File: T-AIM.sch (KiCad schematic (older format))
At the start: 40 parts, among them IC1 ATMEGA328PB-A, J1 ADXL345 Connector, J2 PIR Sensor Connector, J3 JY-MCU HC-05 Pins, J4 CONN_01X03, J5 CONN_01X02, J6 CONN_01X03, SW1 Connection Button, SW2 Reset Button, U1 TPS61200

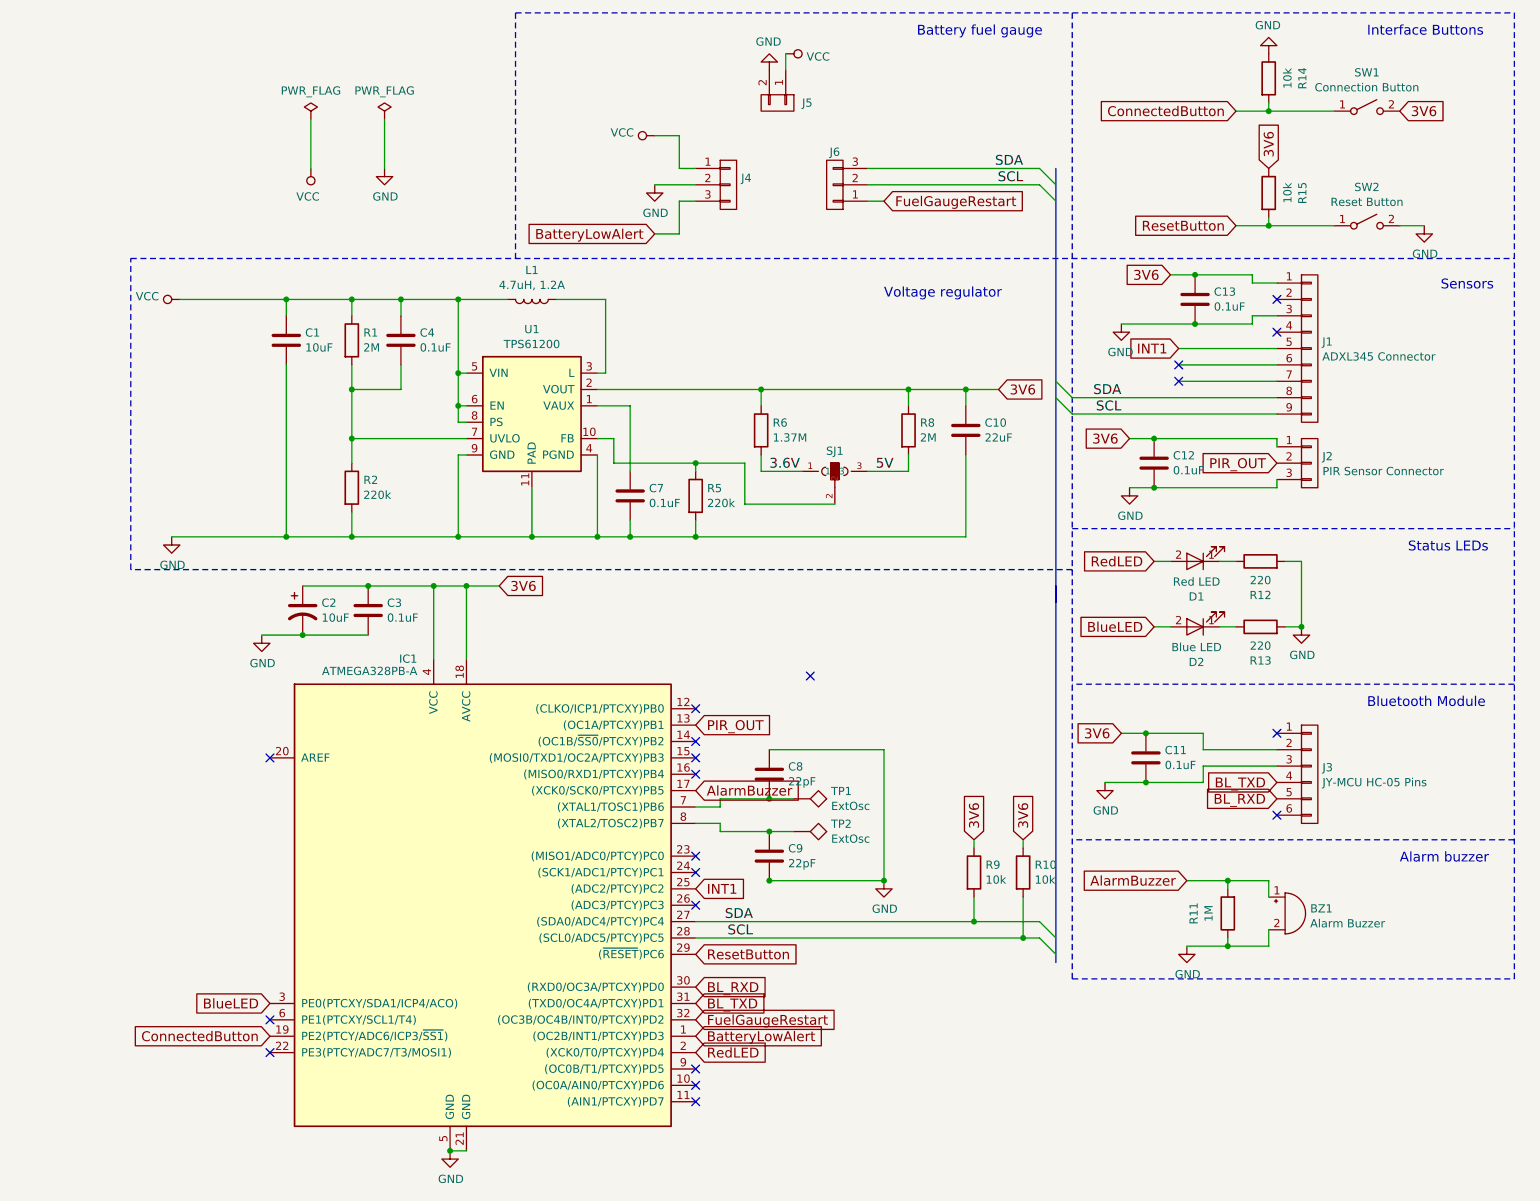
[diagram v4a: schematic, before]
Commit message: v0.3: 3.9V field shrunk; Added ISP header; Fixed fuel gauge pin shortcut :P
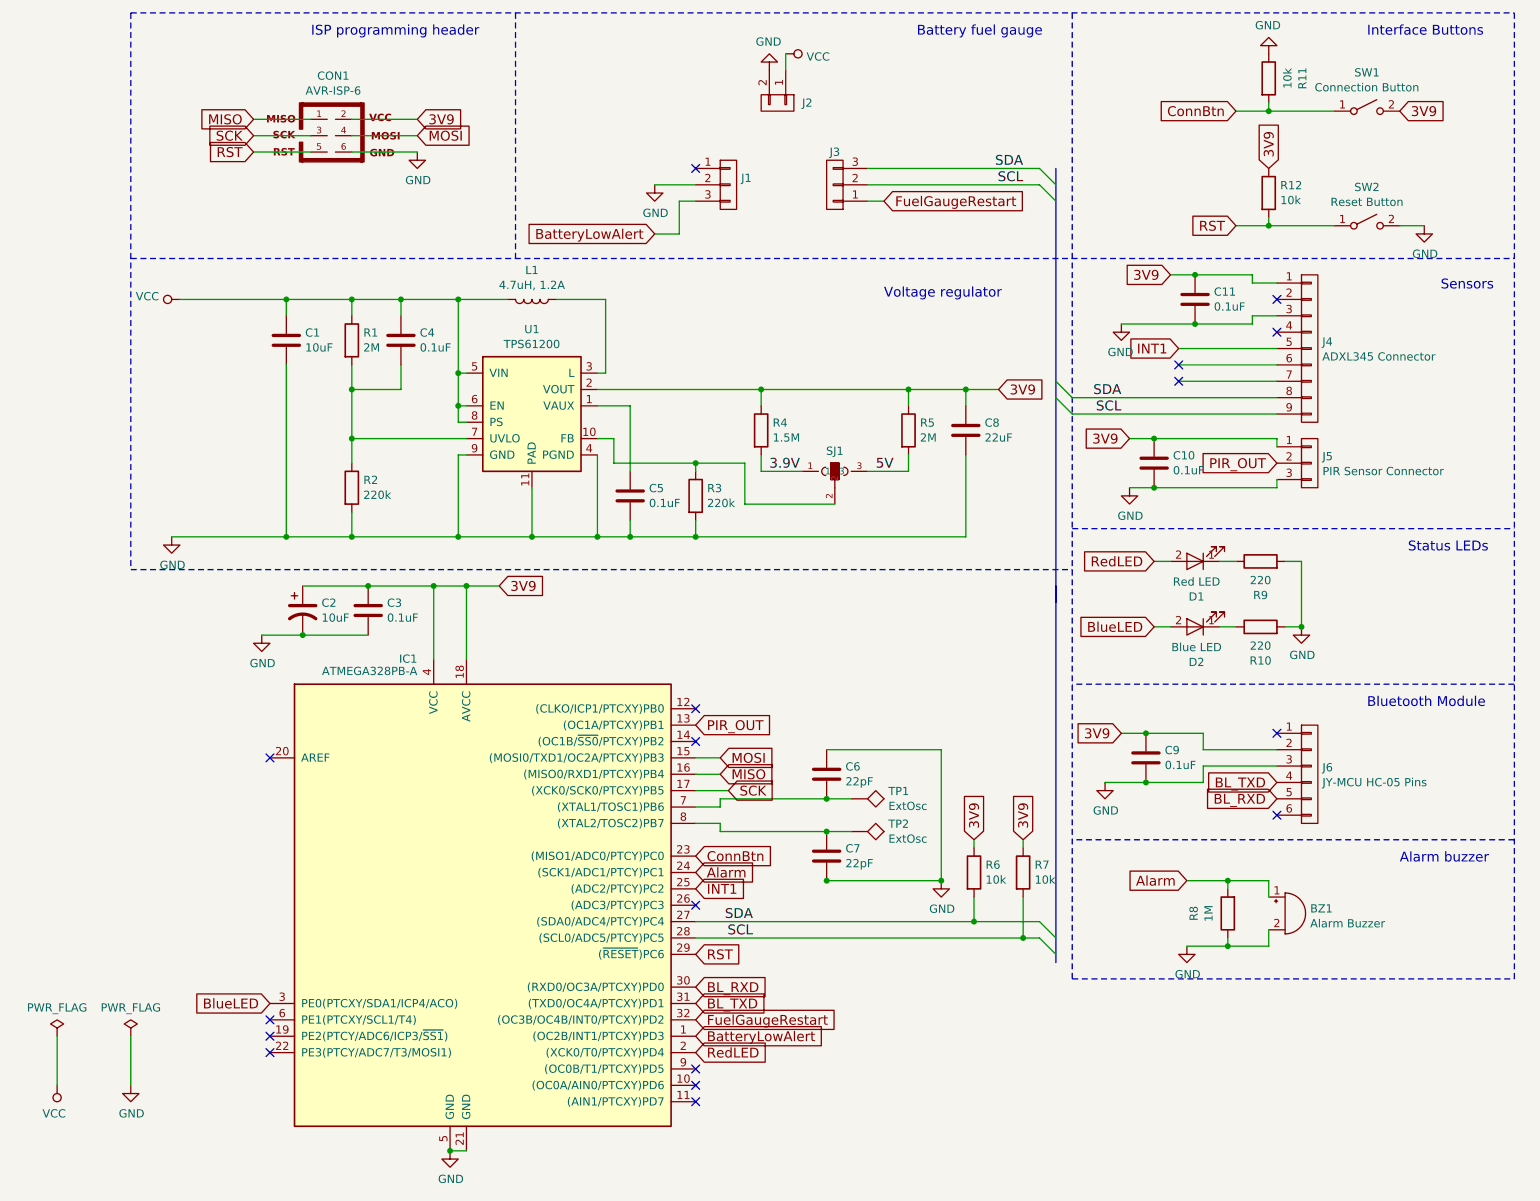
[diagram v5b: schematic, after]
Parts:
- added CON1: AVR-ISP-6, T-AIM:2X3-SHROUDED, symbol AVR-ISP-6
- C1, C3, C4: footprint Capacitors_SMD:C_1812_HandSoldering -> Capacitors_SMD:C_1206_HandSoldering
- C10: renamed from C12; footprint Capacitors_SMD:C_1812_HandSoldering -> Capacitors_SMD:C_1206_HandSoldering
- C11: renamed from C13; footprint Capacitors_SMD:C_1812_HandSoldering -> Capacitors_SMD:C_1206_HandSoldering
- C5: renamed from C7; footprint Capacitors_SMD:C_1812_HandSoldering -> Capacitors_SMD:C_1206_HandSoldering
- C6: renamed from C8; footprint Capacitors_SMD:C_1812_HandSoldering -> Capacitors_SMD:C_0603_HandSoldering
- C7: renamed from C9; footprint Capacitors_SMD:C_1812_HandSoldering -> Capacitors_SMD:C_0603_HandSoldering
- C8: renamed from C10; footprint Capacitors_SMD:C_1812_HandSoldering -> Capacitors_SMD:C_1206_HandSoldering
- C9: renamed from C11; footprint Capacitors_SMD:C_1812_HandSoldering -> Capacitors_SMD:C_1210_HandSoldering
- J6: renamed from J3; footprint Pin_Headers:Pin_Header_Straight_1x06_Pitch2.00mm -> Pin_Headers:Pin_Header_Straight_1x06_Pitch2.54mm
- R10: renamed from R13; footprint Resistors_SMD:R_0805_HandSoldering -> Resistors_SMD:R_1206_HandSoldering
- R11: renamed from R14; footprint Resistors_SMD:R_0805_HandSoldering -> Resistors_SMD:R_1206_HandSoldering
- R12: renamed from R15; footprint Resistors_SMD:R_0805_HandSoldering -> Resistors_SMD:R_1206_HandSoldering
- R4: renamed from R6; value 1.37M -> 1.5M
- R6: renamed from R9; footprint Resistors_SMD:R_0805_HandSoldering -> Resistors_SMD:R_1206_HandSoldering
- R7: renamed from R10; footprint Resistors_SMD:R_0805_HandSoldering -> Resistors_SMD:R_1206_HandSoldering
- R9: renamed from R12; footprint Resistors_SMD:R_0805_HandSoldering -> Resistors_SMD:R_1206_HandSoldering
- TP1, TP2: footprint Connectors:PINTST -> Pin_Headers:Pin_Header_Straight_1x01_Pitch2.54mm
- renumbered J4 to J1, J5 to J2, J6 to J3, J1 to J4, J2 to J5, R5 to R3, R8 to R5, R11 to R8
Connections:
- net GND: now also CON1.6
- net VCC: no longer J1.1 (P1)
- net MOSI: now reaches IC1.15 ((MOSI0/TXD1/OC2A/PTCXY)PB3)
- net MOSI: now also CON1.4
- net MISO: now reaches IC1.16 ((MISO0/RXD1/PTCXY)PB4)
- net MISO: now also CON1.1
- net ConnBtn: now reaches IC1.23 ((MISO1/ADC0/PTCY)PC0)
- net ConnBtn: now also R11.2, SW1.1 (A)
- net Alarm: now reaches IC1.24 ((SCK1/ADC1/PTCY)PC1)
- net Alarm: now also BZ1.1 (-), R8.2
- net 3.6V renamed 3.9V
- net 3V6 renamed 3V9
- net 3V9: now also CON1.2
- removed net AlarmBuzzer: BZ1.1 (-), IC1.17 ((XCK0/SCK0/PTCXY)PB5), R8.2
- removed net ConnectedButton: IC1.19 (PE2(PTCY/ADC6/ICP3/~SS1~)), R11.2, SW1.1 (A)
- net ResetButton renamed RST
- net RST: now also CON1.5
- new net SCK: CON1.3, IC1.17 ((XCK0/SCK0/PTCXY)PB5)
- no-connect marks 20 -> 17
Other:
- note added: "ISP programming header"
- moved on the sheet: C6, C7, TP1, TP2

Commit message: T-AIM v0.3 Final? (Hah): Fixed a C9 footprint from 1210 -> 1206; Updated the script in Gerbers directory to add copper markings (Try script first in command line with -h/--help parameter)
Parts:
- C9: footprint Capacitors_SMD:C_1210_HandSoldering -> Capacitors_SMD:C_1206_HandSoldering
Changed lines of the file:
@@
 F 0 "C9" H 7715 5196 50  0000 L CNN
 F 1 "0.1uF" H 7715 5105 50  0000 L CNN
-F 2 "Capacitors_SMD:C_1210_HandSoldering" H 4688 2550 50  0001 C CNN
+F 2 "Capacitors_SMD:C_1206_HandSoldering" H 4688 2550 50  0001 C CNN
 F 3 "http://www.samsungsem.com/kr/support/library/product-catalog/__icsFiles/afieldfile/2016/09/27/MLCC.pdf" H 4650 2700 50  0001 C CNN
 	1    7600 5150
